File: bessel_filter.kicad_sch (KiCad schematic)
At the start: 10 parts, among them J1 Conn_Coaxial, J2 Conn_Coaxial

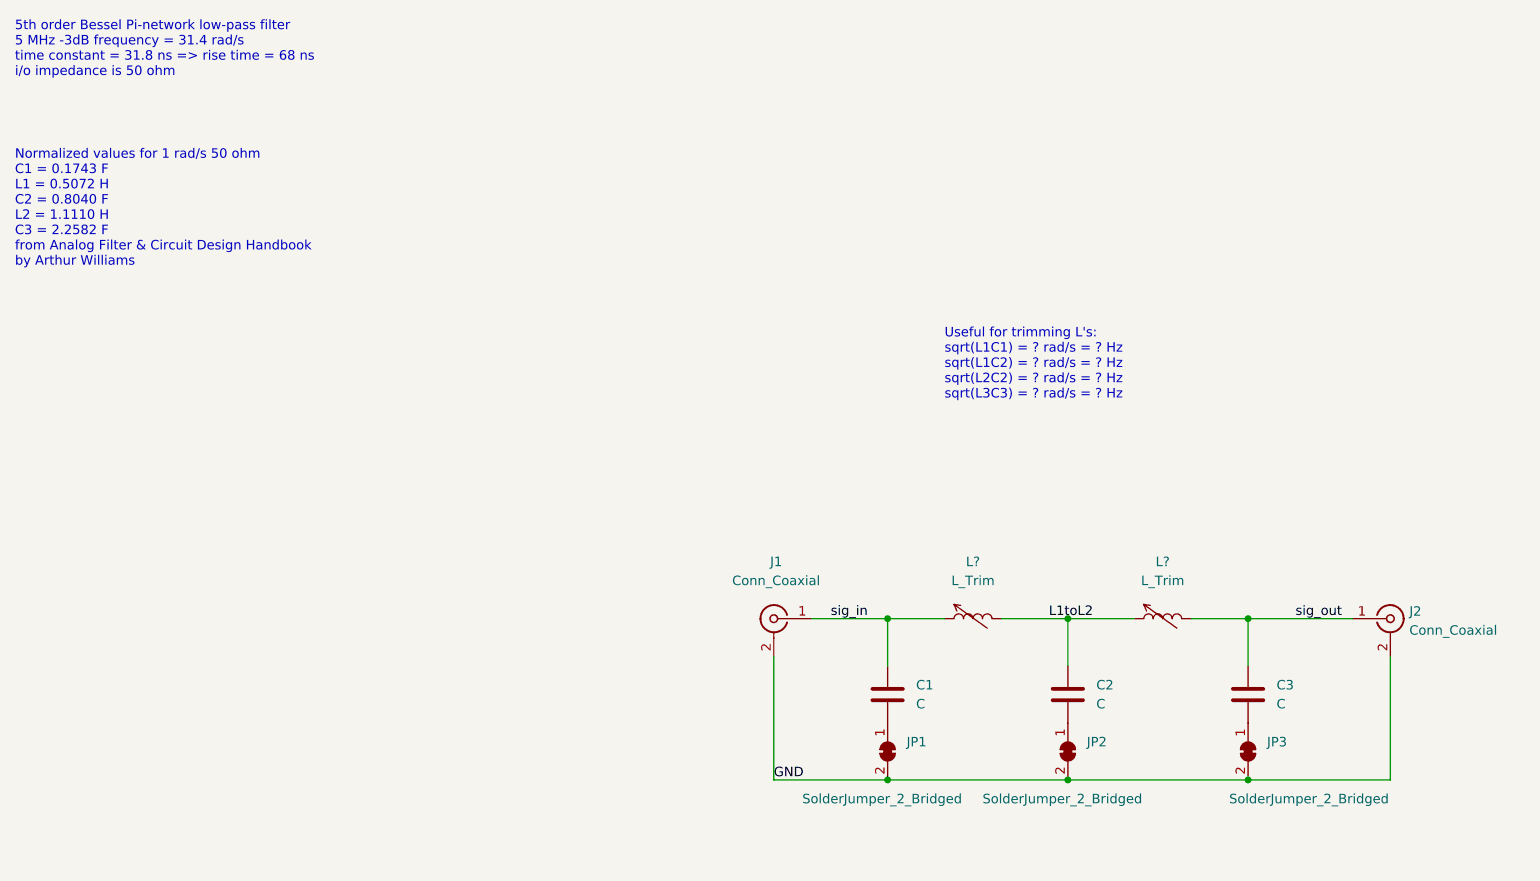
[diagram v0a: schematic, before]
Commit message: added scaled L/C values
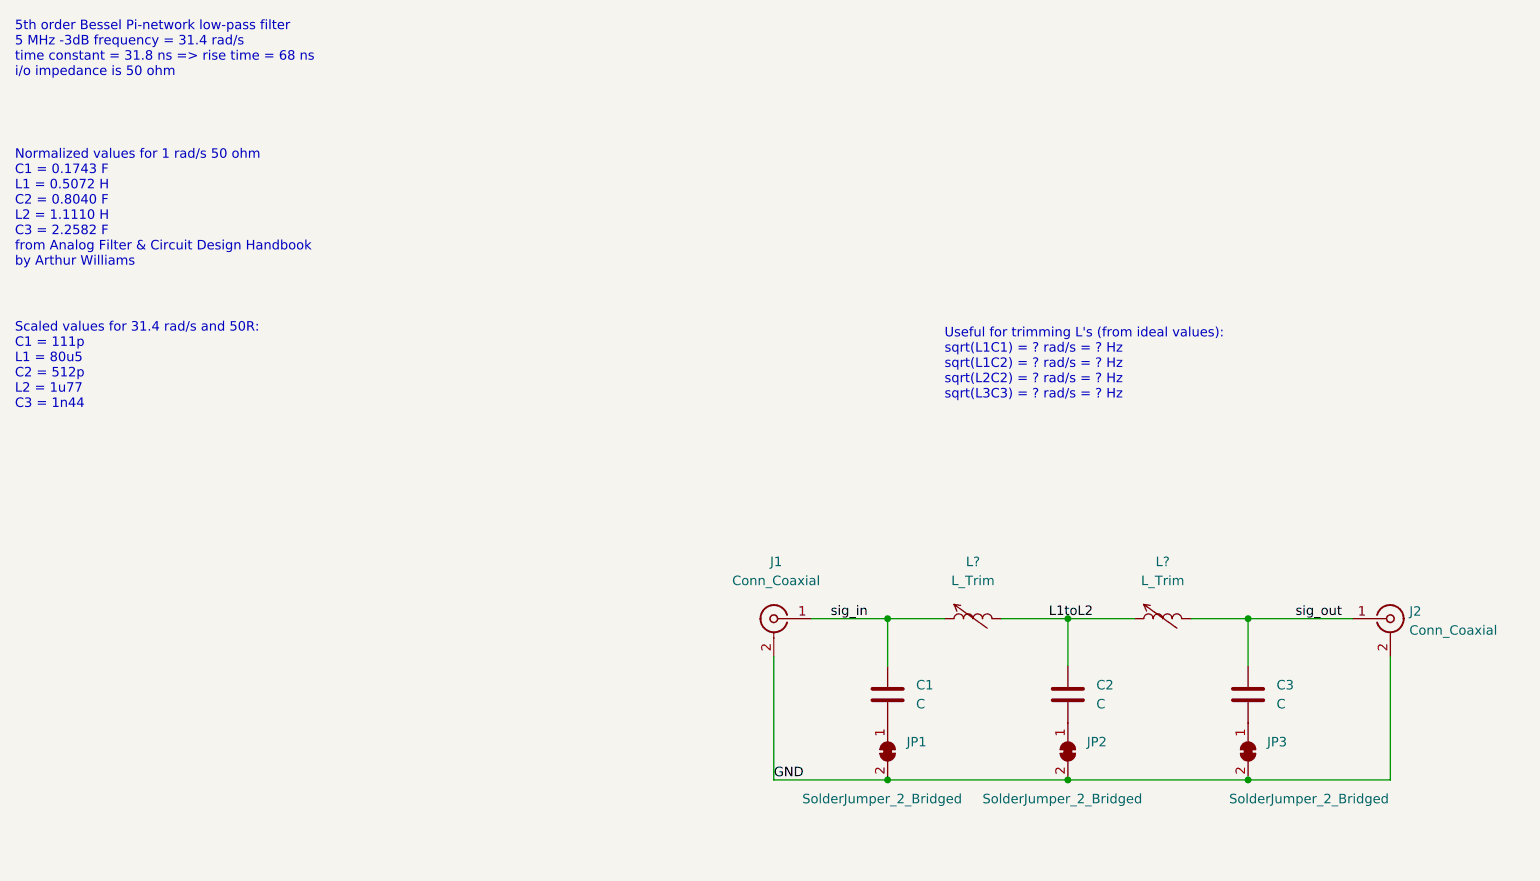
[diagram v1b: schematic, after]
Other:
- note added: "Scaled values for 31.4 rad/s and 50R: C1 = 111p L1 = 80u5 C2 = 512p L2 = 1u77 C3 = 1n44"
- note added: "Useful for trimming L's (from ideal values): sqrt(L1C1) = ? rad/s = ? Hz sqrt(L1C2) = ? rad/s = ? Hz sqrt(L2C2) = ? rad/s = ? Hz sqrt(L3C3) = ? rad/s = ? Hz"
- note removed: "Useful for trimming L's: sqrt(L1C1) = ? rad/s = ? Hz sqrt(L1C2) = ? rad/s = ? Hz sqrt(L2C2) = ? rad/s = ? Hz sqrt(L3C3) = ? rad/s = ? Hz"
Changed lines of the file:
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@@
     (stroke (width 0) (type default) (color 0 0 0 0))
+  )
+  (text "Scaled values for 31.4 rad/s and 50R:\nC1 = 111p\nL1 = 80u5\nC2 = 512p\nL2 = 1u77\nC3 = 1n44"
+    (at 12.7 64.77 0)
+    (effects (font (size 1.27 1.27)) (justify left bottom))
   )
   (text "5th order Bessel Pi-network low-pass filter\n5 MHz -3dB frequency = 31.4 rad/s\ntime constant = 31.8 ns => rise time = 68 ns\ni/o impedance is 50 ohm"
@@
     (effects (font (size 1.27 1.27)) (justify left bottom))
   )
-  (text "Useful for trimming L's:\nsqrt(L1C1) = ? rad/s = ? Hz\nsqrt(L1C2) = ? rad/s = ? Hz\nsqrt(L2C2) = ? rad/s = ? Hz\nsqrt(L3C3) = ? rad/s = ? Hz"
+  (text "Useful for trimming L's (from ideal values):\nsqrt(L1C1) = ? rad/s = ? Hz\nsqrt(L1C2) = ? rad/s = ? Hz\nsqrt(L2C2) = ? rad/s = ? Hz\nsqrt(L3C3) = ? rad/s = ? Hz"
     (at 137.16 63.5 0)
     (effects (font (size 1.27 1.27)) (justify left bottom))

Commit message: Added README
 with info
 fixed L1 value in schematic
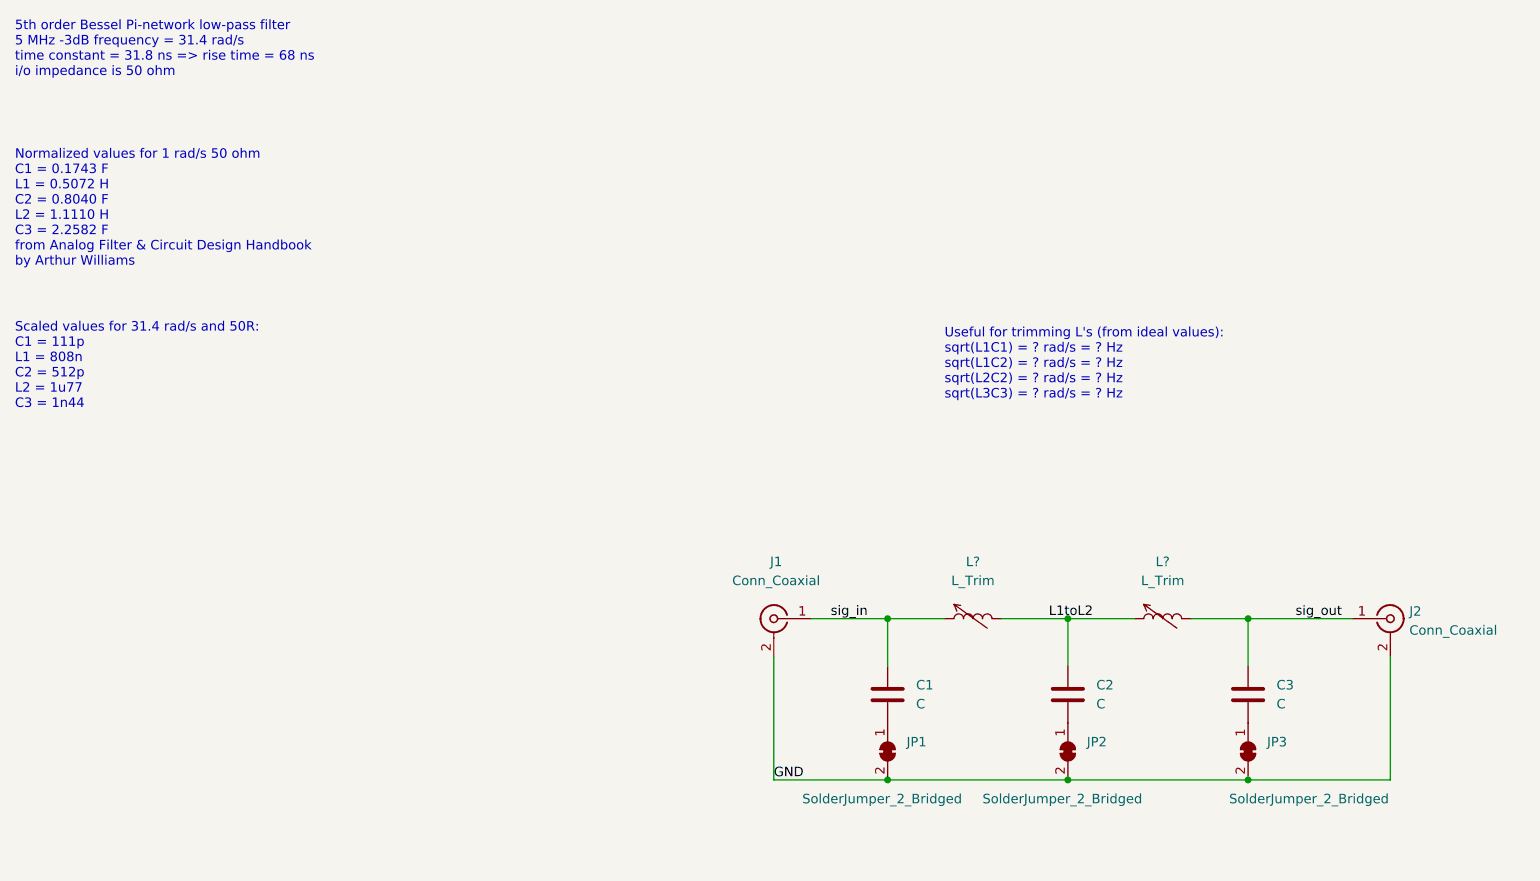
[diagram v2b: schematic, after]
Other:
- note added: "Scaled values for 31.4 rad/s and 50R: C1 = 111p L1 = 808n C2 = 512p L2 = 1u77 C3 = 1n44"
- note removed: "Scaled values for 31.4 rad/s and 50R: C1 = 111p L1 = 80u5 C2 = 512p L2 = 1u77 C3 = 1n44"
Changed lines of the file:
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@@
     (stroke (width 0) (type default) (color 0 0 0 0))
   )
-  (text "Scaled values for 31.4 rad/s and 50R:\nC1 = 111p\nL1 = 80u5\nC2 = 512p\nL2 = 1u77\nC3 = 1n44"
+  (text "Scaled values for 31.4 rad/s and 50R:\nC1 = 111p\nL1 = 808n\nC2 = 512p\nL2 = 1u77\nC3 = 1n44"
     (at 12.7 64.77 0)
     (effects (font (size 1.27 1.27)) (justify left bottom))

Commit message: switched to 3rd order filter for simplicity
  component values are moved from schematic to README.md
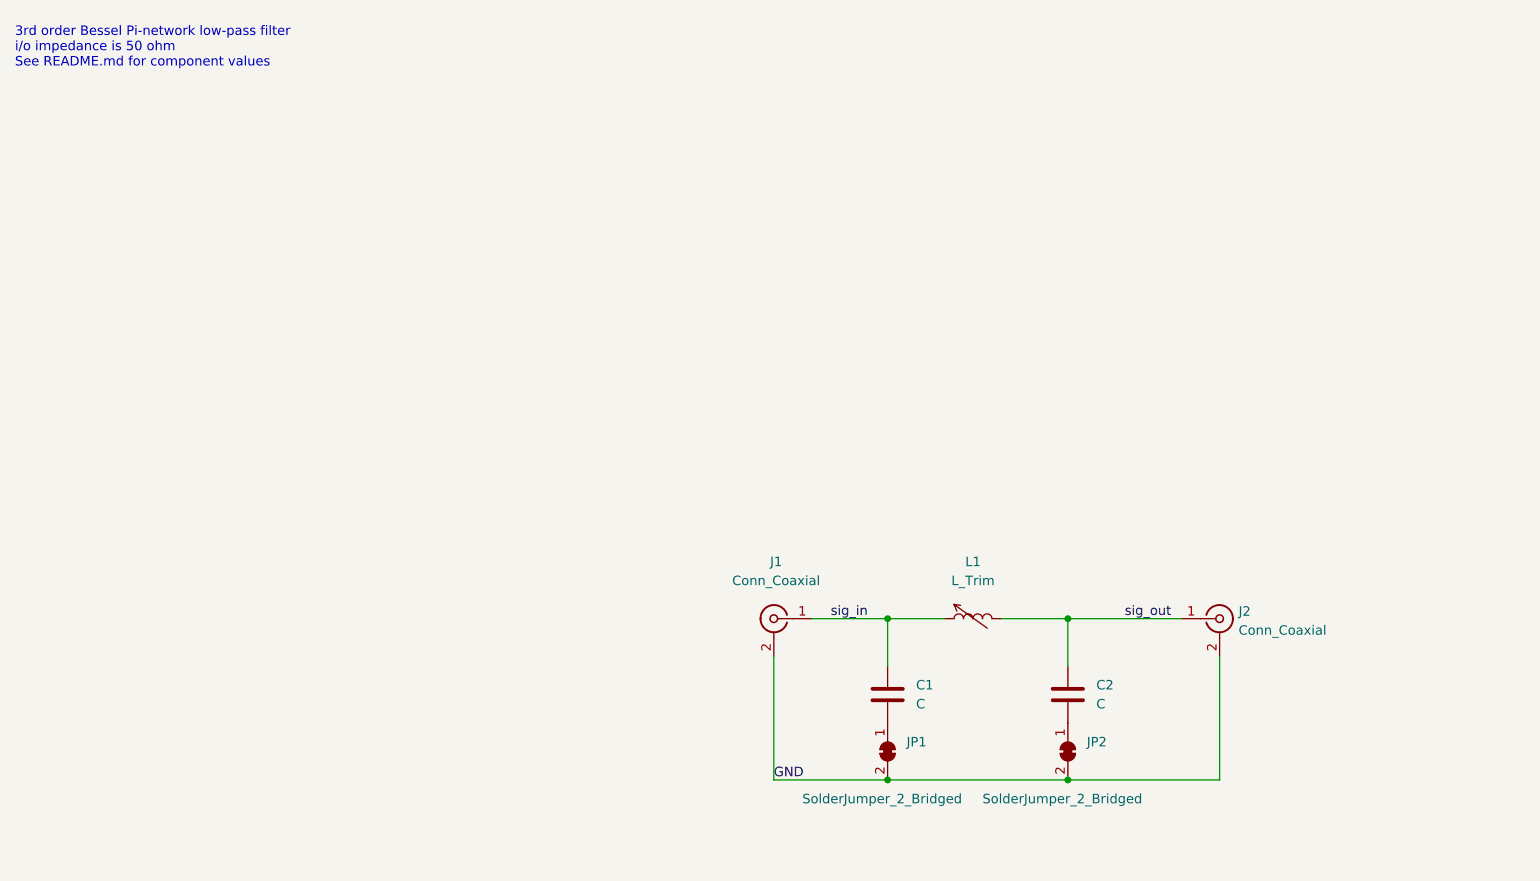
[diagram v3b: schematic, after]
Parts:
- removed C3: C, symbol Device:C
- removed JP3: SolderJumper_2_Bridged, symbol Jumper:SolderJumper_2_Bridged
- removed L?: L_Trim, symbol Device:L_Trim
- gave numbers to parts that had none: 1
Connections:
- net L1toL2 is gone; now on net sig_out: C2.1, L1.2
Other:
- note added: "3rd order Bessel Pi-network low-pass filter i/o impedance is 50 ohm See README.md for component values"
- note removed: "5th order Bessel Pi-network low-pass filter 5 MHz -3dB frequency = 31.4 rad/s time constant = 31.8 ns => rise time = 68 ns i/o impedance is 50 ohm"
- note removed: "Normalized values for 1 rad/s 50 ohm C1 = 0.1743 F L1 = 0.5072 H C2 = 0.8040 F L2 = 1.1110 H C3 = 2.2582 F from Analog Filter & Circuit Design Handbook by Arthur Williams"
- note removed: "Scaled values for 31.4 rad/s and 50R: C1 = 111p L1 = 808n C2 = 512p L2 = 1u77 C3 = 1n44"
- note removed: "Useful for trimming L's (from ideal values): sqrt(L1C1) = ? rad/s = ? Hz sqrt(L1C2) = ? rad/s = ? Hz sqrt(L2C2) = ? rad/s = ? Hz sqrt(L3C3) = ? rad/s = ? Hz"
- moved on the sheet: J2
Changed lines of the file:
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@@
   (title_block
     (title "Bessel Filter")
-    (date "2022-03-10")
+    (date "2022-03-12")
     (rev "0.1")
     (company "HugonLabs")
@@
   (junction (at 153.67 114.3) (diameter 0) (color 0 0 0 0)
   )
-  (junction (at 177.8 114.3) (diameter 0) (color 0 0 0 0)
-  )
-  (junction (at 177.8 92.71) (diameter 0) (color 0 0 0 0)
-  )
   (wire (pts (xy 119.38 92.71) (xy 129.54 92.71))
-    (stroke (width 0) (type default) (color 0 0 0 0))
-  )
-  (wire (pts (xy 177.8 114.3) (xy 196.85 114.3))
     (stroke (width 0) (type default) (color 0 0 0 0))
   )
@@
     (stroke (width 0) (type default) (color 0 0 0 0))
   )
-  (wire (pts (xy 196.85 114.3) (xy 196.85 97.79))
+  (wire (pts (xy 173.99 114.3) (xy 173.99 97.79))
     (stroke (width 0) (type default) (color 0 0 0 0))
   )
-  (wire (pts (xy 177.8 92.71) (xy 191.77 92.71))
+  (wire (pts (xy 153.67 92.71) (xy 168.91 92.71))
     (stroke (width 0) (type default) (color 0 0 0 0))
   )
-  (wire (pts (xy 170.18 92.71) (xy 177.8 92.71))
-    (stroke (width 0) (type default) (color 0 0 0 0))
-  )
-  (wire (pts (xy 153.67 114.3) (xy 177.8 114.3))
+  (wire (pts (xy 153.67 114.3) (xy 173.99 114.3))
     (stroke (width 0) (type default) (color 0 0 0 0))
   )
   (wire (pts (xy 114.3 97.79) (xy 114.3 114.3))
-    (stroke (width 0) (type default) (color 0 0 0 0))
-  )
-  (wire (pts (xy 177.8 92.71) (xy 177.8 99.06))
-    (stroke (width 0) (type default) (color 0 0 0 0))
-  )
-  (wire (pts (xy 153.67 92.71) (xy 162.56 92.71))
     (stroke (width 0) (type default) (color 0 0 0 0))
   )
@@
     (stroke (width 0) (type default) (color 0 0 0 0))
   )
-  (text "Scaled values for 31.4 rad/s and 50R:\nC1 = 111p\nL1 = 808n\nC2 = 512p\nL2 = 1u77\nC3 = 1n44"
-    (at 12.7 64.77 0)
-    (effects (font (size 1.27 1.27)) (justify left bottom))
-  )
-  (text "5th order Bessel Pi-network low-pass filter\n5 MHz -3dB frequency = 31.4 rad/s\ntime constant = 31.8 ns => rise time = 68 ns\ni/o impedance is 50 ohm"
-    (at 12.7 20.32 0)
-    (effects (font (size 1.27 1.27)) (justify left bottom))
-  )
-  (text "Useful for trimming L's (from ideal values):\nsqrt(L1C1) = ? rad/s = ? Hz\nsqrt(L1C2) = ? rad/s = ? Hz\nsqrt(L2C2) = ? rad/s = ? Hz\nsqrt(L3C3) = ? rad/s = ? Hz"
-    (at 137.16 63.5 0)
-    (effects (font (size 1.27 1.27)) (justify left bottom))
-  )
-  (text "Normalized values for 1 rad/s 50 ohm\nC1 = 0.1743 F\nL1 = 0.5072 H\nC2 = 0.8040 F\nL2 = 1.1110 H\nC3 = 2.2582 F\nfrom Analog Filter & Circuit Design Handbook\nby Arthur Williams"
-    (at 12.7 45.72 0)
+  (text "3rd order Bessel Pi-network low-pass filter\ni/o impedance is 50 ohm\nSee README.md for component values"
+    (at 12.7 19.05 0)
     (effects (font (size 1.27 1.27)) (justify left bottom))
   )
@@
     (effects (font (size 1.27 1.27)) (justify left bottom))
   )
-  (label "L1toL2" (at 151.13 92.71 0)
-    (effects (font (size 1.27 1.27)) (justify left bottom))
-  )
   (label "GND" (at 114.3 114.3 0)
     (effects (font (size 1.27 1.27)) (justify left bottom))
   )
-  (label "sig_out" (at 184.15 92.71 0)
+  (label "sig_out" (at 161.29 92.71 0)
     (effects (font (size 1.27 1.27)) (justify left bottom))
   )
@@
     )
     (property "Datasheet" "~" (id 3) (at 153.67 102.87 0)
-      (effects (font (size 1.27 1.27)) hide)
-    )
-    (pin "1")
-    (pin "2")
-  )
-  (symbol (lib_id "Jumper:SolderJumper_2_Bridged") (at 177.8 110.49 270) (unit 1)
-    (in_bom yes) (on_board yes)
-    (property "Reference" "JP3" (id 0) (at 180.34 109.2199 90)
-      (effects (font (size 1.27 1.27)) (justify left))
-    )
-    (property "Value" "SolderJumper_2_Bridged" (id 1) (at 175.26 116.84 90)
-      (effects (font (size 1.27 1.27)) (justify left))
-    )
-    (property "Footprint" "" (id 2) (at 177.8 110.49 0)
-      (effects (font (size 1.27 1.27)) hide)
-    )
-    (property "Datasheet" "~" (id 3) (at 177.8 110.49 0)
       (effects (font (size 1.27 1.27)) hide)
     )
@@
   (symbol (lib_id "Device:L_Trim") (at 140.97 92.71 90) (unit 1)
     (in_bom yes) (on_board yes) (fields_autoplaced)
-    (property "Reference" "L?" (id 0) (at 140.97 85.09 90))
+    (property "Reference" "L1" (id 0) (at 140.97 85.09 90))
     (property "Value" "L_Trim" (id 1) (at 140.97 87.63 90))
     (property "Footprint" "" (id 2) (at 140.97 92.71 0)
@@
     )
     (property "Datasheet" "~" (id 3) (at 140.97 92.71 0)
-      (effects (font (size 1.27 1.27)) hide)
-    )
-    (pin "1")
-    (pin "2")
-  )
-  (symbol (lib_id "Device:C") (at 177.8 102.87 0) (unit 1)
-    (in_bom yes) (on_board yes) (fields_autoplaced)
-    (property "Reference" "C3" (id 0) (at 181.61 101.5999 0)
-      (effects (font (size 1.27 1.27)) (justify left))
-    )
-    (property "Value" "C" (id 1) (at 181.61 104.1399 0)
-      (effects (font (size 1.27 1.27)) (justify left))
-    )
-    (property "Footprint" "" (id 2) (at 178.7652 106.68 0)
-      (effects (font (size 1.27 1.27)) hide)
-    )
-    (property "Datasheet" "~" (id 3) (at 177.8 102.87 0)
       (effects (font (size 1.27 1.27)) hide)
     )
@@
     (pin "2")
   )
-  (symbol (lib_id "Device:L_Trim") (at 166.37 92.71 90) (unit 1)
-    (in_bom yes) (on_board yes) (fields_autoplaced)
-    (property "Reference" "L?" (id 0) (at 166.37 85.09 90))
-    (property "Value" "L_Trim" (id 1) (at 166.37 87.63 90))
-    (property "Footprint" "" (id 2) (at 166.37 92.71 0)
-      (effects (font (size 1.27 1.27)) hide)
-    )
-    (property "Datasheet" "~" (id 3) (at 166.37 92.71 0)
-      (effects (font (size 1.27 1.27)) hide)
-    )
-    (pin "1")
-    (pin "2")
-  )
   (symbol (lib_id "Device:C") (at 129.54 102.87 0) (unit 1)
     (in_bom yes) (on_board yes) (fields_autoplaced)
@@
     (pin "2")
   )
-  (symbol (lib_id "Connector:Conn_Coaxial") (at 196.85 92.71 0) (unit 1)
+  (symbol (lib_id "Connector:Conn_Coaxial") (at 173.99 92.71 0) (unit 1)
     (in_bom yes) (on_board yes) (fields_autoplaced)
-    (property "Reference" "J2" (id 0) (at 199.39 91.7331 0)
+    (property "Reference" "J2" (id 0) (at 176.53 91.7331 0)
       (effects (font (size 1.27 1.27)) (justify left))
     )
-    (property "Value" "Conn_Coaxial" (id 1) (at 199.39 94.2731 0)
+    (property "Value" "Conn_Coaxial" (id 1) (at 176.53 94.2731 0)
       (effects (font (size 1.27 1.27)) (justify left))
     )
-    (property "Footprint" "" (id 2) (at 196.85 92.71 0)
+    (property "Footprint" "" (id 2) (at 173.99 92.71 0)
       (effects (font (size 1.27 1.27)) hide)
     )
-    (property "Datasheet" " ~" (id 3) (at 196.85 92.71 0)
+    (property "Datasheet" " ~" (id 3) (at 173.99 92.71 0)
       (effects (font (size 1.27 1.27)) hide)
     )
@@
       (reference "C2") (unit 1) (value "C") (footprint "")
     )
-    (path "/88b981ae-9bdb-41f9-8dbe-d622d981265d"
-      (reference "C3") (unit 1) (value "C") (footprint "")
-    )
     (path "/90d228ac-5ec9-4302-b393-9e4058ef8745"
       (reference "J1") (unit 1) (value "Conn_Coaxial") (footprint "")
@@
       (reference "JP2") (unit 1) (value "SolderJumper_2_Bridged") (footprint "")
     )
-    (path "/48b47fbf-434f-46cc-821d-9b551b0a5714"
-      (reference "JP3") (unit 1) (value "SolderJumper_2_Bridged") (footprint "")
-    )
     (path "/867a4a3d-7555-41bb-964a-c09677a9fea2"
-      (reference "L?") (unit 1) (value "L_Trim") (footprint "")
-    )
-    (path "/a544ba87-1a8d-4c4a-8eed-d40a07f6113b"
-      (reference "L?") (unit 1) (value "L_Trim") (footprint "")
+      (reference "L1") (unit 1) (value "L_Trim") (footprint "")
     )
   )
